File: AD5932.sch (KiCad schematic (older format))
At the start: 11 parts, among them U1 BGA2851, U2 AD5932

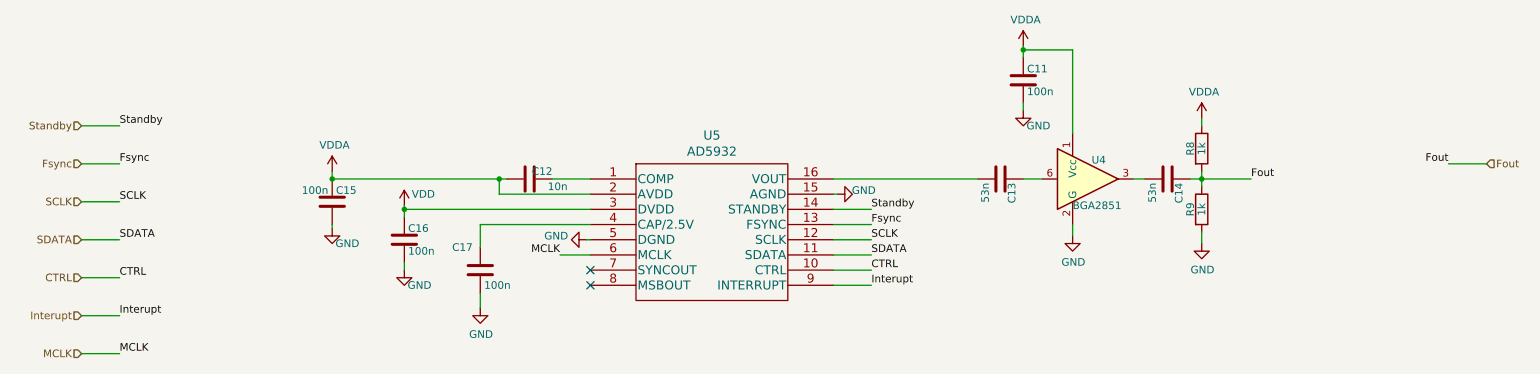
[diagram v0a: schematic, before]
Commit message: Implemented the LMH6881 instead of the AD8000 Continued routing
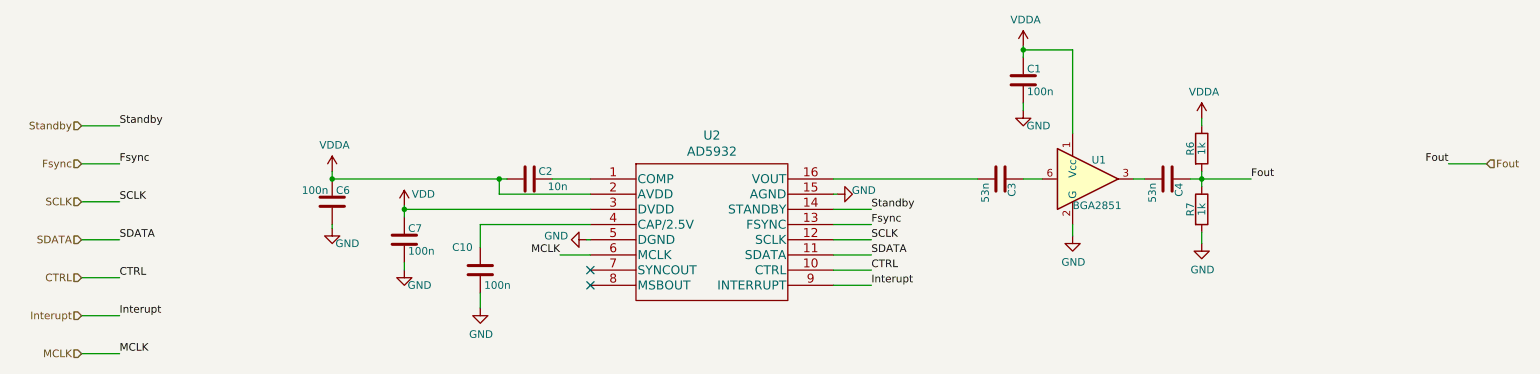
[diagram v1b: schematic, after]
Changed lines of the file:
@@
 AR Path="/61E6DCA9/61C919AC" Ref="U?"  Part="1"
 AR Path="/61E7139B/61C919AC" Ref="U5"  Part="1"
-F 0 "U5" H 5400 3837 60  0000 C CNN
+F 0 "U2" H 5400 3837 60  0000 C CNN
 F 1 "AD5932" H 5400 3731 60  0000 C CNN
 F 2 "Package_SO:TSSOP-16_4.4x5mm_P0.65mm" H 5500 3740 60  0001 C CNN
@@
 AR Path="/61E6DCA9/61C919B8" Ref="C?"  Part="1"
 AR Path="/61E7139B/61C919B8" Ref="C17"  Part="1"
-F 0 "C17" H 3825 3600 50  0000 R CNN
+F 0 "C10" H 3825 3600 50  0000 R CNN
 F 1 "100n" H 4075 3350 50  0000 R CNN
 F 2 "Capacitor_SMD:C_0603_1608Metric_Pad1.08x0.95mm_HandSolder" H 3913 3300 50  0001 C CNN
@@
 AR Path="/61E6DCA9/61C919BF" Ref="#PWR?"  Part="1"
 AR Path="/61E7139B/61C919BF" Ref="#PWR029"  Part="1"
-F 0 "#PWR029" H 3875 3450 50  0001 C CNN
+F 0 "#PWR017" H 3875 3450 50  0001 C CNN
 F 1 "GND" H 3880 3527 50  0000 C CNN
 F 2 "" H 3875 3700 50  0001 C CNN
@@
 AR Path="/61E6DCA9/61C919C7" Ref="C?"  Part="1"
 AR Path="/61E7139B/61C919C7" Ref="C16"  Part="1"
-F 0 "C16" H 3400 3325 50  0000 L CNN
+F 0 "C7" H 3400 3325 50  0000 L CNN
 F 1 "100n" H 3400 3175 50  0000 L CNN
 F 2 "Capacitor_SMD:C_0603_1608Metric_Pad1.08x0.95mm_HandSolder" H 3413 3100 50  0001 C CNN
@@
 AR Path="/61E6DCA9/61C919CD" Ref="#PWR?"  Part="1"
 AR Path="/61E7139B/61C919CD" Ref="#PWR028"  Part="1"
-F 0 "#PWR028" H 3375 3200 50  0001 C CNN
+F 0 "#PWR016" H 3375 3200 50  0001 C CNN
 F 1 "GND" H 3475 3350 50  0000 C CNN
 F 2 "" H 3375 3450 50  0001 C CNN
@@
 AR Path="/61E6DCA9/61C919D5" Ref="C?"  Part="1"
 AR Path="/61E7139B/61C919D5" Ref="C12"  Part="1"
-F 0 "C12" V 4150 3000 50  0000 R CNN
+F 0 "C2" V 4150 3000 50  0000 R CNN
 F 1 "10n" V 4250 3100 50  0000 R CNN
 F 2 "Capacitor_SMD:C_0603_1608Metric_Pad1.08x0.95mm_HandSolder" H 4238 2700 50  0001 C CNN
@@
 AR Path="/61E6DCA9/61C919DD" Ref="#PWR?"  Part="1"
 AR Path="/61E7139B/61C919DD" Ref="#PWR026"  Part="1"
-F 0 "#PWR026" H 4575 3000 50  0001 C CNN
+F 0 "#PWR014" H 4575 3000 50  0001 C CNN
 F 1 "GND" V 4550 3050 50  0000 C CNN
 F 2 "" H 4575 3250 50  0001 C CNN
@@
 AR Path="/61E6DCA9/61C919E4" Ref="#PWR?"  Part="1"
 AR Path="/61E7139B/61C919E4" Ref="#PWR022"  Part="1"
-F 0 "#PWR022" H 6225 2700 50  0001 C CNN
+F 0 "#PWR010" H 6225 2700 50  0001 C CNN
 F 1 "GND" V 6250 2775 50  0000 C CNN
 F 2 "" H 6225 2950 50  0001 C CNN
@@
 AR Path="/61E6DCA9/61C919FD" Ref="#PWR?"  Part="1"
 AR Path="/61E7139B/61C919FD" Ref="#PWR021"  Part="1"
-F 0 "#PWR021" H 2900 2650 50  0001 C CNN
+F 0 "#PWR06" H 2900 2650 50  0001 C CNN
 F 1 "VDDA" H 2915 2973 50  0000 C CNN
 F 2 "" H 2900 2800 50  0001 C CNN
@@
 AR Path="/61E6DCA9/61C91A03" Ref="#PWR?"  Part="1"
 AR Path="/61E7139B/61C91A03" Ref="#PWR023"  Part="1"
-F 0 "#PWR023" H 3375 2875 50  0001 C CNN
+F 0 "#PWR011" H 3375 2875 50  0001 C CNN
 F 1 "VDD" H 3500 3100 50  0000 C CNN
 F 2 "" H 3375 3025 50  0001 C CNN
@@
 AR Path="/61E6DCA9/61C91A0A" Ref="C?"  Part="1"
 AR Path="/61E7139B/61C91A0A" Ref="C13"  Part="1"
-F 0 "C13" H 7275 2775 50  0000 R CNN
+F 0 "C3" H 7275 2775 50  0000 R CNN
 F 1 "53n" H 7275 2950 50  0000 R CNN
 F 2 "Capacitor_SMD:C_0603_1608Metric_Pad1.08x0.95mm_HandSolder" H 7338 2700 50  0001 C CNN
@@
 AR Path="/61E6DCA9/61C91A10" Ref="C?"  Part="1"
 AR Path="/61E7139B/61C91A10" Ref="C15"  Part="1"
-F 0 "C15" H 2925 3075 50  0000 L CNN
+F 0 "C6" H 2925 3075 50  0000 L CNN
 F 1 "100n" H 2700 3075 50  0000 L CNN
 F 2 "Capacitor_SMD:C_0603_1608Metric_Pad1.08x0.95mm_HandSolder" H 2938 2850 50  0001 C CNN
@@
 AR Path="/61E6DCA9/61C91A16" Ref="#PWR?"  Part="1"
 AR Path="/61E7139B/61C91A16" Ref="#PWR024"  Part="1"
-F 0 "#PWR024" H 2900 2925 50  0001 C CNN
+F 0 "#PWR012" H 2900 2925 50  0001 C CNN
 F 1 "GND" H 3000 3075 50  0000 C CNN
 F 2 "" H 2900 3175 50  0001 C CNN
@@
 AR Path="/61E6DCA9/61CC9808" Ref="R?"  Part="1"
 AR Path="/61E7139B/61CC9808" Ref="R8"  Part="1"
-F 0 "R8" V 8550 2650 50  0000 C CNN
+F 0 "R6" V 8550 2650 50  0000 C CNN
 F 1 "1k" V 8625 2650 50  0000 C CNN
 F 2 "Resistor_SMD:R_0603_1608Metric_Pad0.98x0.95mm_HandSolder" V 8555 2650 50  0001 C CNN
@@
 AR Path="/61E6DCA9/61CC980E" Ref="R?"  Part="1"
 AR Path="/61E7139B/61CC980E" Ref="R9"  Part="1"
-F 0 "R9" V 8550 3050 50  0000 C CNN
+F 0 "R7" V 8550 3050 50  0000 C CNN
 F 1 "1k" V 8625 3050 50  0000 C CNN
 F 2 "Resistor_SMD:R_0603_1608Metric_Pad0.98x0.95mm_HandSolder" V 8555 3050 50  0001 C CNN
@@
 AR Path="/61E6DCA9/61CC9819" Ref="#PWR?"  Part="1"
 AR Path="/61E7139B/61CC9819" Ref="#PWR027"  Part="1"
-F 0 "#PWR027" H 8625 3025 50  0001 C CNN
+F 0 "#PWR015" H 8625 3025 50  0001 C CNN
 F 1 "GND" H 8630 3102 50  0000 C CNN
 F 2 "" H 8625 3275 50  0001 C CNN
@@
 AR Path="/61E6DCA9/61CC9820" Ref="#PWR?"  Part="1"
 AR Path="/61E7139B/61CC9820" Ref="#PWR020"  Part="1"
-F 0 "#PWR020" H 8625 2300 50  0001 C CNN
+F 0 "#PWR05" H 8625 2300 50  0001 C CNN
 F 1 "VDDA" H 8640 2623 50  0000 C CNN
 F 2 "" H 8625 2450 50  0001 C CNN
@@
 AR Path="/61E6DCA9/61CC9827" Ref="U?"  Part="1"
 AR Path="/61E7139B/61CC9827" Ref="U4"  Part="1"
-F 0 "U4" H 7900 2975 50  0000 L CNN
+F 0 "U1" H 7900 2975 50  0000 L CNN
 F 1 "BGA2851" H 7775 2675 50  0000 L CNN
 F 2 "Package_TO_SOT_SMD:SOT-363_SC-70-6" H 7825 2200 50  0001 C CNN
@@
 AR Path="/61E6DCA9/61CC982F" Ref="C?"  Part="1"
 AR Path="/61E7139B/61CC982F" Ref="C14"  Part="1"
-F 0 "C14" H 8375 2775 50  0000 R CNN
+F 0 "C4" H 8375 2775 50  0000 R CNN
 F 1 "53n" H 8375 2950 50  0000 R CNN
 F 2 "Capacitor_SMD:C_0603_1608Metric_Pad1.08x0.95mm_HandSolder" H 8438 2700 50  0001 C CNN
@@
 AR Path="/61E6DCA9/61CC9836" Ref="#PWR?"  Part="1"
 AR Path="/61E7139B/61CC9836" Ref="#PWR025"  Part="1"
-F 0 "#PWR025" H 7775 2975 50  0001 C CNN
+F 0 "#PWR013" H 7775 2975 50  0001 C CNN
 F 1 "GND" H 7780 3052 50  0000 C CNN
 F 2 "" H 7775 3225 50  0001 C CNN
@@
 AR Path="/61E6DCA9/61CC983C" Ref="C?"  Part="1"
 AR Path="/61E7139B/61CC983C" Ref="C11"  Part="1"
-F 0 "C11" H 7475 2275 50  0000 L CNN
+F 0 "C1" H 7475 2275 50  0000 L CNN
 F 1 "100n" H 7475 2125 50  0000 L CNN
 F 2 "Capacitor_SMD:C_0603_1608Metric_Pad1.08x0.95mm_HandSolder" H 7488 2050 50  0001 C CNN
@@
 AR Path="/61E6DCA9/61CC9842" Ref="#PWR?"  Part="1"
 AR Path="/61E7139B/61CC9842" Ref="#PWR019"  Part="1"
-F 0 "#PWR019" H 7450 2150 50  0001 C CNN
+F 0 "#PWR02" H 7450 2150 50  0001 C CNN
 F 1 "GND" H 7550 2300 50  0000 C CNN
 F 2 "" H 7450 2400 50  0001 C CNN
@@
 AR Path="/61E6DCA9/61CC984E" Ref="#PWR?"  Part="1"
 AR Path="/61E7139B/61CC984E" Ref="#PWR018"  Part="1"
-F 0 "#PWR018" H 7450 1825 50  0001 C CNN
+F 0 "#PWR01" H 7450 1825 50  0001 C CNN
 F 1 "VDDA" H 7465 2148 50  0000 C CNN
 F 2 "" H 7450 1975 50  0001 C CNN

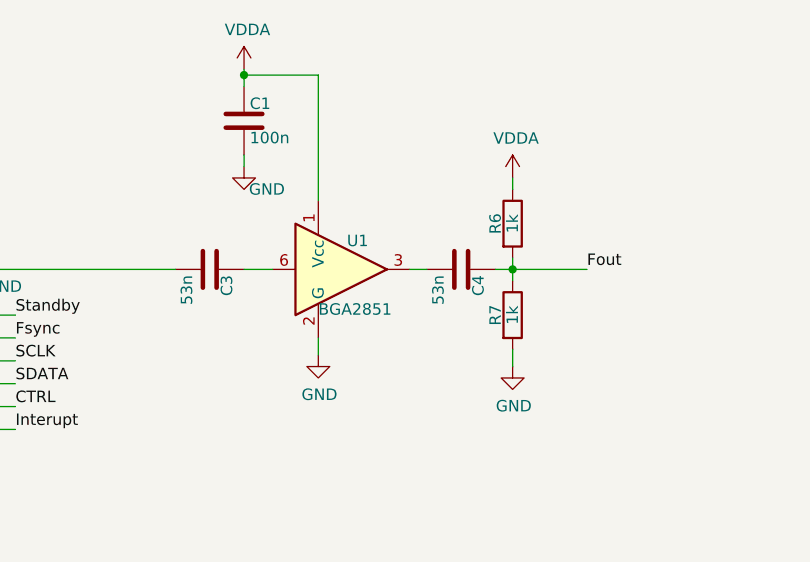
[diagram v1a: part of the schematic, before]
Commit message: Deleted the fix gain amlifier
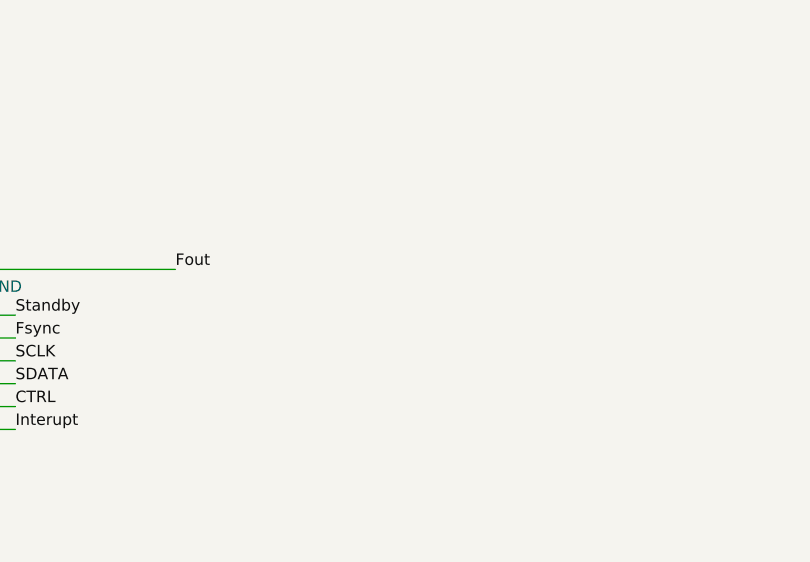
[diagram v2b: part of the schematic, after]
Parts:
- removed C1: 100n, Capacitor_SMD:C_0603_1608Metric_Pad1.08x0.95mm_HandSolder, symbol Device:C
- removed C3, C4: 53n, Capacitor_SMD:C_0603_1608Metric_Pad1.08x0.95mm_HandSolder, symbol Device:C
- removed R6, R7: 1k, Resistor_SMD:R_0603_1608Metric_Pad0.98x0.95mm_HandSolder, symbol Device:R
- removed U1: BGA2851, Package_TO_SOT_SMD:SOT-363_SC-70-6, symbol RF_Amplifier:BGA2851
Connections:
- net Fout: now also U2.16 (VOUT)
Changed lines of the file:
@@
-$Comp
-L Device:C C?
-U 1 1 61C91A0A
-P 7300 2850
-AR Path="/60D21B6E/61C91A0A" Ref="C?"  Part="1"
-AR Path="/61C91A0A" Ref="C?"  Part="1"
-AR Path="/61C59087/61C91A0A" Ref="C3"  Part="1"
-AR Path="/61E6DCA9/61C91A0A" Ref="C?"  Part="1"
-AR Path="/61E7139B/61C91A0A" Ref="C13"  Part="1"
-F 0 "C3" H 7275 2775 50  0000 R CNN
-F 1 "53n" H 7275 2950 50  0000 R CNN
-F 2 "Capacitor_SMD:C_0603_1608Metric_Pad1.08x0.95mm_HandSolder" H 7338 2700 50  0001 C CNN
-F 3 "~" H 7300 2850 50  0001 C CNN
-	1    7300 2850
-	0    -1   -1   0
-$EndComp
 $Comp
 L Device:C C?
@@
 Wire Wire Line
 	4000 2850 2900 2850
-$Comp
-L Device:R R?
-U 1 1 61CC9808
-P 8625 2650
-AR Path="/61CC9808" Ref="R?"  Part="1"
-AR Path="/61C59087/61CC9808" Ref="R6"  Part="1"
-AR Path="/61E6DCA9/61CC9808" Ref="R?"  Part="1"
-AR Path="/61E7139B/61CC9808" Ref="R8"  Part="1"
-F 0 "R6" V 8550 2650 50  0000 C CNN
-F 1 "1k" V 8625 2650 50  0000 C CNN
-F 2 "Resistor_SMD:R_0603_1608Metric_Pad0.98x0.95mm_HandSolder" V 8555 2650 50  0001 C CNN
-F 3 "~" H 8625 2650 50  0001 C CNN
-	1    8625 2650
-	1    0    0    -1
-$EndComp
-$Comp
-L Device:R R?
-U 1 1 61CC980E
-P 8625 3050
-AR Path="/61CC980E" Ref="R?"  Part="1"
-AR Path="/61C59087/61CC980E" Ref="R7"  Part="1"
-AR Path="/61E6DCA9/61CC980E" Ref="R?"  Part="1"
-AR Path="/61E7139B/61CC980E" Ref="R9"  Part="1"
-F 0 "R7" V 8550 3050 50  0000 C CNN
-F 1 "1k" V 8625 3050 50  0000 C CNN
-F 2 "Resistor_SMD:R_0603_1608Metric_Pad0.98x0.95mm_HandSolder" V 8555 3050 50  0001 C CNN
-F 3 "~" H 8625 3050 50  0001 C CNN
-	1    8625 3050
-	1    0    0    -1
-$EndComp
-Wire Wire Line
-	8550 2850 8625 2850
-Wire Wire Line
-	8625 2800 8625 2850
-Connection ~ 8625 2850
-Wire Wire Line
-	8625 2850 8950 2850
-Wire Wire Line
-	8625 2850 8625 2900
-$Comp
-L power:GND #PWR?
-U 1 1 61CC9819
-P 8625 3275
-AR Path="/60D21B6E/61CC9819" Ref="#PWR?"  Part="1"
-AR Path="/61CC9819" Ref="#PWR?"  Part="1"
-AR Path="/61C59087/61CC9819" Ref="#PWR015"  Part="1"
-AR Path="/61E6DCA9/61CC9819" Ref="#PWR?"  Part="1"
-AR Path="/61E7139B/61CC9819" Ref="#PWR027"  Part="1"
-F 0 "#PWR015" H 8625 3025 50  0001 C CNN
-F 1 "GND" H 8630 3102 50  0000 C CNN
-F 2 "" H 8625 3275 50  0001 C CNN
-F 3 "" H 8625 3275 50  0001 C CNN
-	1    8625 3275
-	1    0    0    -1
-$EndComp
-Wire Wire Line
-	8625 3200 8625 3275
-$Comp
-L power:VDDA #PWR?
-U 1 1 61CC9820
-P 8625 2450
-AR Path="/61CC9820" Ref="#PWR?"  Part="1"
-AR Path="/61C59087/61CC9820" Ref="#PWR05"  Part="1"
-AR Path="/61E6DCA9/61CC9820" Ref="#PWR?"  Part="1"
-AR Path="/61E7139B/61CC9820" Ref="#PWR020"  Part="1"
-F 0 "#PWR05" H 8625 2300 50  0001 C CNN
-F 1 "VDDA" H 8640 2623 50  0000 C CNN
-F 2 "" H 8625 2450 50  0001 C CNN
-F 3 "" H 8625 2450 50  0001 C CNN
-	1    8625 2450
-	1    0    0    -1
-$EndComp
-Wire Wire Line
-	8625 2450 8625 2500
-$Comp
-L RF_Amplifier:BGA2851 U?
-U 1 1 61CC9827
-P 7875 2850
-AR Path="/61CC9827" Ref="U?"  Part="1"
-AR Path="/61C59087/61CC9827" Ref="U1"  Part="1"
-AR Path="/61E6DCA9/61CC9827" Ref="U?"  Part="1"
-AR Path="/61E7139B/61CC9827" Ref="U4"  Part="1"
-F 0 "U1" H 7900 2975 50  0000 L CNN
-F 1 "BGA2851" H 7775 2675 50  0000 L CNN
-F 2 "Package_TO_SOT_SMD:SOT-363_SC-70-6" H 7825 2200 50  0001 C CNN
-F 3 "https://www.nxp.com/docs/en/data-sheet/BGA2851.pdf" H 7875 2850 50  0001 C CNN
-	1    7875 2850
-	1    0    0    -1
-$EndComp
-Wire Wire Line
-	8175 2850 8250 2850
-Wire Wire Line
-	7450 2850 7575 2850
-$Comp
-L Device:C C?
-U 1 1 61CC982F
-P 8400 2850
-AR Path="/60D21B6E/61CC982F" Ref="C?"  Part="1"
-AR Path="/61CC982F" Ref="C?"  Part="1"
-AR Path="/61C59087/61CC982F" Ref="C4"  Part="1"
-AR Path="/61E6DCA9/61CC982F" Ref="C?"  Part="1"
-AR Path="/61E7139B/61CC982F" Ref="C14"  Part="1"
-F 0 "C4" H 8375 2775 50  0000 R CNN
-F 1 "53n" H 8375 2950 50  0000 R CNN
-F 2 "Capacitor_SMD:C_0603_1608Metric_Pad1.08x0.95mm_HandSolder" H 8438 2700 50  0001 C CNN
-F 3 "~" H 8400 2850 50  0001 C CNN
-	1    8400 2850
-	0    -1   -1   0
-$EndComp
-Wire Wire Line
-	7775 3150 7775 3225
-$Comp
-L power:GND #PWR?
-U 1 1 61CC9836
-P 7775 3225
-AR Path="/60D21B6E/61CC9836" Ref="#PWR?"  Part="1"
-AR Path="/61CC9836" Ref="#PWR?"  Part="1"
-AR Path="/61C59087/61CC9836" Ref="#PWR013"  Part="1"
-AR Path="/61E6DCA9/61CC9836" Ref="#PWR?"  Part="1"
-AR Path="/61E7139B/61CC9836" Ref="#PWR025"  Part="1"
-F 0 "#PWR013" H 7775 2975 50  0001 C CNN
-F 1 "GND" H 7780 3052 50  0000 C CNN
-F 2 "" H 7775 3225 50  0001 C CNN
-F 3 "" H 7775 3225 50  0001 C CNN
-	1    7775 3225
-	1    0    0    -1
-$EndComp
-$Comp
-L Device:C C?
-U 1 1 61CC983C
-P 7450 2200
-AR Path="/61CC983C" Ref="C?"  Part="1"
-AR Path="/6188E6DD/61CC983C" Ref="C?"  Part="1"
-AR Path="/61C59087/61CC983C" Ref="C1"  Part="1"
-AR Path="/61E6DCA9/61CC983C" Ref="C?"  Part="1"
-AR Path="/61E7139B/61CC983C" Ref="C11"  Part="1"
-F 0 "C1" H 7475 2275 50  0000 L CNN
-F 1 "100n" H 7475 2125 50  0000 L CNN
-F 2 "Capacitor_SMD:C_0603_1608Metric_Pad1.08x0.95mm_HandSolder" H 7488 2050 50  0001 C CNN
-F 3 "~" H 7450 2200 50  0001 C CNN
-	1    7450 2200
-	1    0    0    -1
-$EndComp
-$Comp
-L power:GND #PWR?
-U 1 1 61CC9842
-P 7450 2400
-AR Path="/60D21B6E/61CC9842" Ref="#PWR?"  Part="1"
-AR Path="/61CC9842" Ref="#PWR?"  Part="1"
-AR Path="/6188E6DD/61CC9842" Ref="#PWR?"  Part="1"
-AR Path="/61C59087/61CC9842" Ref="#PWR02"  Part="1"
-AR Path="/61E6DCA9/61CC9842" Ref="#PWR?"  Part="1"
-AR Path="/61E7139B/61CC9842" Ref="#PWR019"  Part="1"
-F 0 "#PWR02" H 7450 2150 50  0001 C CNN
-F 1 "GND" H 7550 2300 50  0000 C CNN
-F 2 "" H 7450 2400 50  0001 C CNN
-F 3 "" H 7450 2400 50  0001 C CNN
-	1    7450 2400
-	1    0    0    -1
-$EndComp
-Wire Wire Line
-	7450 2050 7450 2000
-Connection ~ 7450 2000
-Wire Wire Line
-	7450 2350 7450 2400
-Wire Wire Line
-	7450 1975 7450 2000
-Wire Wire Line
-	7775 2550 7775 2000
-Wire Wire Line
-	7450 2000 7775 2000
-$Comp
-L power:VDDA #PWR?
-U 1 1 61CC984E
-P 7450 1975
-AR Path="/61CC984E" Ref="#PWR?"  Part="1"
-AR Path="/61C59087/61CC984E" Ref="#PWR01"  Part="1"
-AR Path="/61E6DCA9/61CC984E" Ref="#PWR?"  Part="1"
-AR Path="/61E7139B/61CC984E" Ref="#PWR018"  Part="1"
-F 0 "#PWR01" H 7450 1825 50  0001 C CNN
-F 1 "VDDA" H 7465 2148 50  0000 C CNN
-F 2 "" H 7450 1975 50  0001 C CNN
-F 3 "" H 7450 1975 50  0001 C CNN
-	1    7450 1975
-	1    0    0    -1
-$EndComp
 Text HLabel 1250 2500 0    50   Input ~ 0
 Standby
@@
 Wire Wire Line
 	3875 3150 4600 3150
-Text Label 8950 2850 0    50   ~ 0
+Text Label 7150 2850 0    50   ~ 0
 Fout
 $EndSCHEMATC
